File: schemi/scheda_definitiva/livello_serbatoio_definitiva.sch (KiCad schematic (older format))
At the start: 43 parts, among them J1 USB_B, J2 BTN_LED_GROUP, J3 CONN_LCD, J4 CONN_US, J5 ICSP, J6 Exp_Analog_2, J7 Exp_Analog, SW1 SW_RST, U1 FT232RL, U2 ATmega328P-PU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

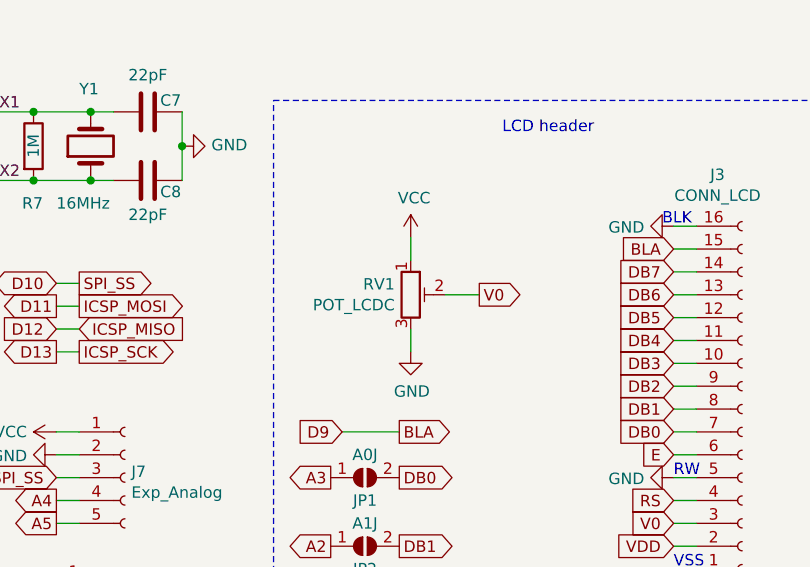
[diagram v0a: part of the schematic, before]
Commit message: spostato LCD e rifatto modello box - LCD centrato su LCD - revisione layout - nuovo modello box (box + coperchio + pulsante + assembly scheda e lcd) - aggiornate immagini prototipo - creati file stl (box e coperchio)  per preventivazione stampa 3d
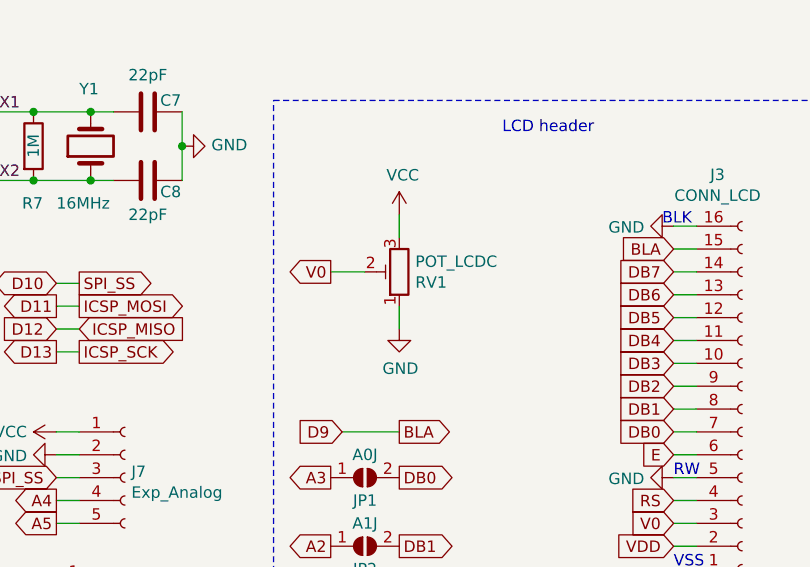
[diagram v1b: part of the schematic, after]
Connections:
- net GND: now also RV1.1; no longer RV1.3
- net VCC: now also RV1.3; no longer RV1.1
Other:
- moved on the sheet: RV1
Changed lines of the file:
@@
 L power:VCC #PWR015
 U 1 1 5F56E79B
-P 9100 3200
-F 0 "#PWR015" H 9100 3050 50  0001 C CNN
-F 1 "VCC" H 9115 3373 50  0000 C CNN
-F 2 "" H 9100 3200 50  0001 C CNN
-F 3 "" H 9100 3200 50  0001 C CNN
-	1    9100 3200
+P 9050 3100
+F 0 "#PWR015" H 9050 2950 50  0001 C CNN
+F 1 "VCC" H 9065 3273 50  0000 C CNN
+F 2 "" H 9050 3100 50  0001 C CNN
+F 3 "" H 9050 3100 50  0001 C CNN
+	1    9050 3100
 	1    0    0    -1
 $EndComp
@@
 D5
 Wire Wire Line
-	9100 3600 9100 3700
+	9050 3200 9050 3100
 Wire Wire Line
-	9250 3450 9400 3450
+	8900 3350 8750 3350
 Wire Wire Line
-	9100 3200 9100 3300
-Text GLabel 9400 3450 2    50   Output ~ 0
+	9050 3600 9050 3500
+Text GLabel 8750 3350 0    50   Output ~ 0
 V0
 Wire Wire Line
@@
 L Device:R_POT_TRIM RV1
 U 1 1 5F0B6050
-P 9100 3450
-F 0 "RV1" H 9030 3496 50  0000 R CNN
-F 1 "POT_LCDC" H 9030 3405 50  0000 R CNN
-F 2 "simboli_custom:Trimmer_ACP_470" H 9100 3450 50  0001 C CNN
-F 3 "~" H 9100 3450 50  0001 C CNN
-	1    9100 3450
-	1    0    0    -1
+P 9050 3350
+F 0 "RV1" H 8980 3396 50  0000 R CNN
+F 1 "POT_LCDC" H 8980 3305 50  0000 R CNN
+F 2 "simboli_custom:Trimmer_ACP_470" H 9050 3350 50  0001 C CNN
+F 3 "~" H 9050 3350 50  0001 C CNN
+	1    9050 3350
+	-1   0    0    1
 $EndComp
 $Comp
 L power:GND #PWR016
 U 1 1 5F0B54BC
-P 9100 3700
-F 0 "#PWR016" H 9100 3450 50  0001 C CNN
-F 1 "GND" H 9105 3527 50  0000 C CNN
-F 2 "" H 9100 3700 50  0001 C CNN
-F 3 "" H 9100 3700 50  0001 C CNN
-	1    9100 3700
+P 9050 3600
+F 0 "#PWR016" H 9050 3350 50  0001 C CNN
+F 1 "GND" H 9055 3427 50  0000 C CNN
+F 2 "" H 9050 3600 50  0001 C CNN
+F 3 "" H 9050 3600 50  0001 C CNN
+	1    9050 3600
 	1    0    0    -1
 $EndComp

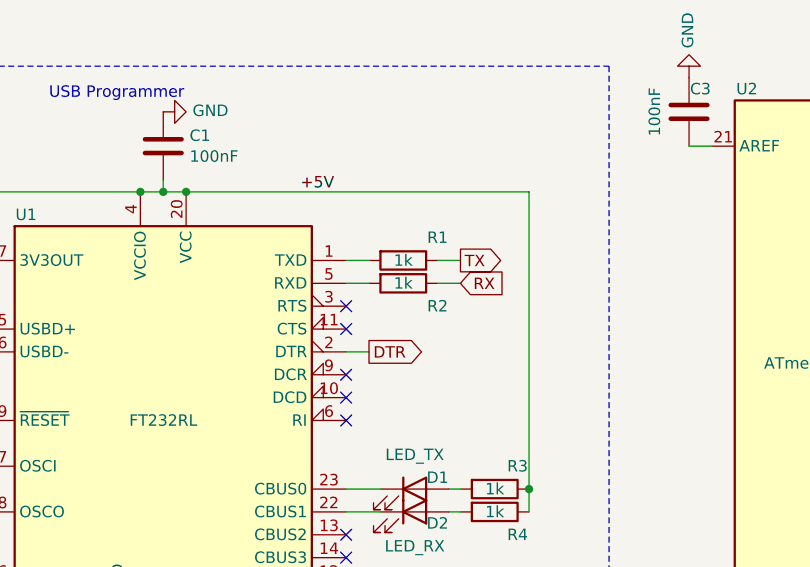
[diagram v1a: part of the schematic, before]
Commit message: aggiunte piazzole CTS/RTS + aggiunte etichette a pin digitali - rivisto gerber - rivista footprint oscillatore
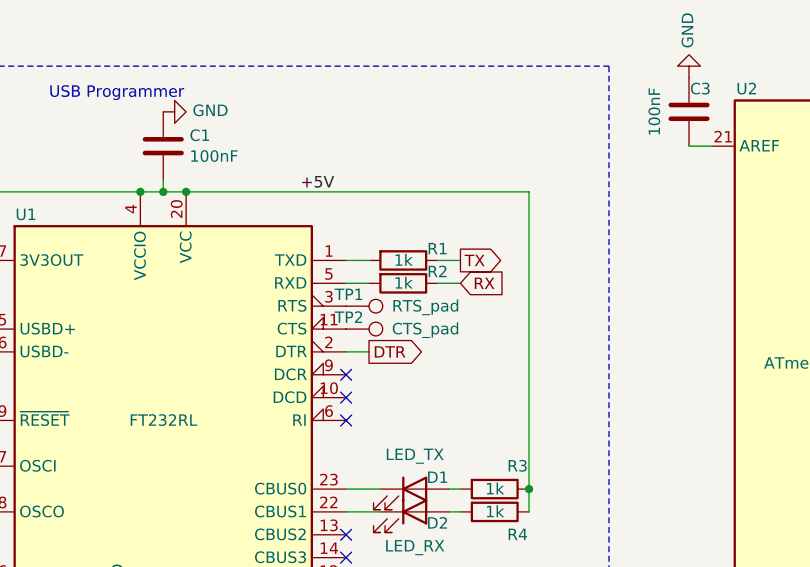
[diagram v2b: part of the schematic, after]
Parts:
- added TP1: RTS_pad, TestPoint:TestPoint_Pad_D1.0mm, symbol Connector:TestPoint
- added TP2: CTS_pad, TestPoint:TestPoint_Pad_D1.0mm, symbol Connector:TestPoint
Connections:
- net at U1.11 (CTS): now also TP2.1
- net at U1.3 (RTS): now also TP1.1
- no-connect marks 10 -> 8
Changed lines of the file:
@@
 Sheet 1 1
 Title "Monitor Serbatoio"
-Date "2020-11-21"
-Rev "1"
+Date "2020-12-27"
+Rev "v1.0_Rev.A"
 Comp ""
-Comment1 ""
+Comment1 "Versione Espandibile"
 Comment2 ""
 Comment3 ""
@@
 U 1 1 5F436A47
 P 4100 2750
-F 0 "R2" V 4200 2900 50  0000 C CNN
+F 0 "R2" V 4050 2900 50  0000 C CNN
 F 1 "1k" V 4100 2750 50  0000 C CNN
 F 2 "Resistor_THT:R_Axial_DIN0309_L9.0mm_D3.2mm_P12.70mm_Horizontal" V 4030 2750 50  0001 C CNN
@@
 U 1 1 5F435E22
 P 4100 2650
-F 0 "R1" V 4000 2800 50  0000 C CNN
+F 0 "R1" V 4050 2800 50  0000 C CNN
 F 1 "1k" V 4100 2650 50  0000 C CNN
 F 2 "Resistor_THT:R_Axial_DIN0309_L9.0mm_D3.2mm_P12.70mm_Horizontal" V 4030 2650 50  0001 C CNN
@@
 	1    0    0    -1
 $EndComp
-NoConn ~ 3850 2850
-NoConn ~ 3850 2950
 NoConn ~ 3850 3150
 NoConn ~ 3850 3250
@@
 Text Notes 7800 700  0    50   ~ 0
 Button + LED
+$Comp
+L Connector:TestPoint TP1
+U 1 1 5FE956AB
+P 3850 2850
+F 0 "TP1" V 3800 2800 50  0000 L CNN
+F 1 "RTS_pad" V 3850 3050 50  0000 L CNN
+F 2 "TestPoint:TestPoint_Pad_D1.0mm" H 4050 2850 50  0001 C CNN
+F 3 "~" H 4050 2850 50  0001 C CNN
+	1    3850 2850
+	0    1    1    0
+$EndComp
+$Comp
+L Connector:TestPoint TP2
+U 1 1 5FE99EB0
+P 3850 2950
+F 0 "TP2" V 3800 2900 50  0000 L CNN
+F 1 "CTS_pad" V 3850 3150 50  0000 L CNN
+F 2 "TestPoint:TestPoint_Pad_D1.0mm" H 4050 2950 50  0001 C CNN
+F 3 "~" H 4050 2950 50  0001 C CNN
+	1    3850 2950
+	0    1    1    0
+$EndComp
 $EndSCHEMATC

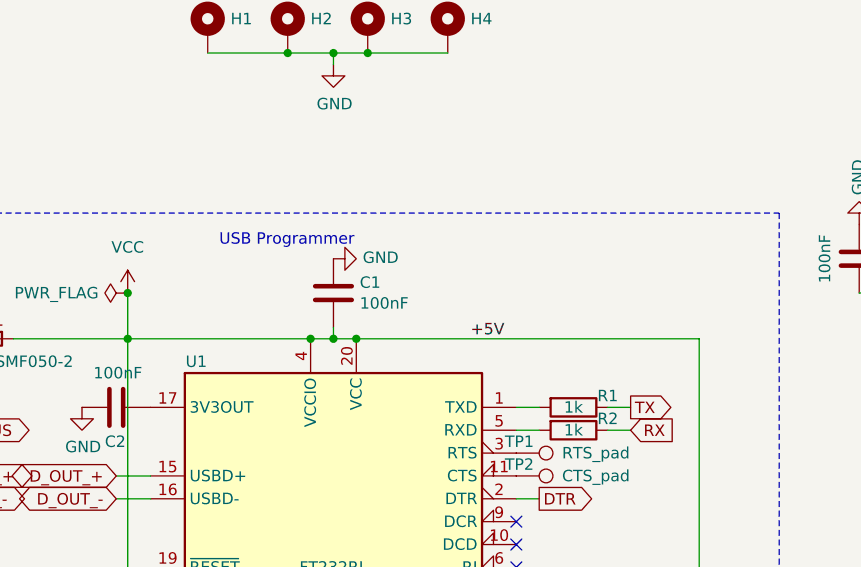
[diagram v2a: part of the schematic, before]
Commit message: modifica per seriale - aggiunto elettrolitico per alimentazione - fix test seriale
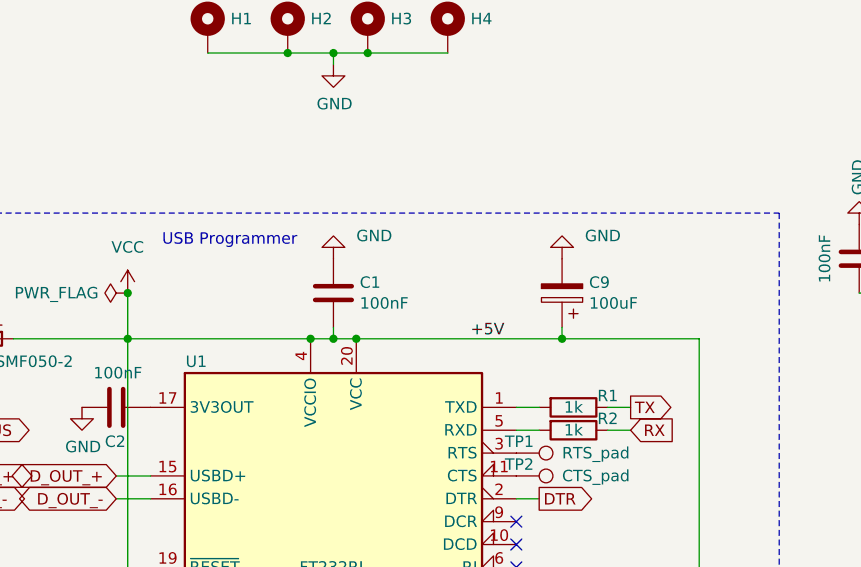
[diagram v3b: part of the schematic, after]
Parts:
- added C9: 100uF, Capacitor_THT:CP_Radial_D5.0mm_P2.00mm, symbol Device:CP
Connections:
- net GND: now also C9.2
- net VCC: now also C9.1
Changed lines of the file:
@@
 Sheet 1 1
 Title "Monitor Serbatoio"
-Date "2020-12-27"
-Rev "v1.0_Rev.A"
+Date "2021-02-13"
+Rev "v1.0_Rev.B"
 Comp ""
 Comment1 "Versione Espandibile"
@@
 Text GLabel 4350 2650 2    50   Output ~ 0
 TX
-Text Notes 2550 1950 0    50   ~ 0
+Text Notes 2300 1950 0    50   ~ 0
 USB Programmer
 Connection ~ 2150 2150
@@
 Wire Wire Line
 	4650 2350 4650 3650
-Wire Wire Line
-	3150 2350 4650 2350
 Wire Wire Line
 	4000 3750 3850 3750
@@
 P 3050 2000
 F 0 "#PWR0104" H 3050 1750 50  0001 C CNN
-F 1 "GND" V 3055 1872 50  0000 R CNN
+F 1 "GND" H 2950 1900 50  0000 R CNN
 F 2 "" H 3050 2000 50  0001 C CNN
 F 3 "" H 3050 2000 50  0001 C CNN
 	1    3050 2000
-	0    -1   -1   0
+	-1   0    0    1
 $EndComp
 $Comp
@@
 	0    1    1    0
 $EndComp
+$Comp
+L Device:CP C9
+U 1 1 60287C39
+P 4050 2150
+F 0 "C9" H 3932 2104 50  0000 R CNN
+F 1 "100uF" H 3932 2195 50  0000 R CNN
+F 2 "Capacitor_THT:CP_Radial_D5.0mm_P2.00mm" H 4088 2000 50  0001 C CNN
+F 3 "~" H 4050 2150 50  0001 C CNN
+	1    4050 2150
+	-1   0    0    1
+$EndComp
+$Comp
+L power:GND #PWR026
+U 1 1 6029B133
+P 4050 2000
+F 0 "#PWR026" H 4050 1750 50  0001 C CNN
+F 1 "GND" H 3950 1900 50  0000 R CNN
+F 2 "" H 4050 2000 50  0001 C CNN
+F 3 "" H 4050 2000 50  0001 C CNN
+	1    4050 2000
+	-1   0    0    1
+$EndComp
+Wire Wire Line
+	3150 2350 4050 2350
+Wire Wire Line
+	4050 2300 4050 2350
+Connection ~ 4050 2350
+Wire Wire Line
+	4050 2350 4650 2350
 $EndSCHEMATC

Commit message: aggiunta ferrite a scheda rev. B
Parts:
- added FB1: MPZ2012, Inductor_SMD:L_0805_2012Metric_Pad1.15x1.40mm_HandSolder, symbol Device:Ferrite_Bead
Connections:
- net VBUS: now also FB1.1; no longer J1.1 (VBUS)
- new net: FB1.2, J1.1 (VBUS)
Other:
- moved on the sheet: F1
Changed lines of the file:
@@
 	0    -1   -1   0
 $EndComp
-Wire Wire Line
-	1250 2750 1300 2750
-Connection ~ 1300 2750
-Wire Wire Line
-	1300 2350 1300 2750
 $Comp
 L Device:R R9
@@
 DTR
 Wire Wire Line
-	1650 2350 2150 2350
-Wire Wire Line
 	2150 2150 2150 2350
 NoConn ~ 2250 3750
@@
 Wire Wire Line
 	2250 3350 2150 3350
-Wire Wire Line
-	1300 2350 1350 2350
 $Comp
 L Device:C C2
@@
 Text GLabel 1350 3050 2    50   BiDi ~ 0
 D_IN_-
-Text GLabel 1400 2750 2    50   BiDi ~ 0
-VBUS
 Text GLabel 2100 2950 0    50   BiDi ~ 0
 D_OUT_+
@@
 Text GLabel 2050 5700 2    50   BiDi ~ 0
 D_OUT_-
-Wire Wire Line
-	1300 2750 1400 2750
 Wire Wire Line
 	1250 2950 1350 2950
@@
 L Device:Polyfuse F1
 U 1 1 5FB200DA
-P 1500 2350
-F 0 "F1" V 1400 2350 50  0000 C CNN
-F 1 "MF-MSMF050-2" V 1600 2500 50  0000 C CNN
-F 2 "simboli_custom:MF-MSMF_1812_4532Metric_Pad1.30x3.40mm_HandSolder" H 1550 2150 50  0001 L CNN
-F 3 "~" H 1500 2350 50  0001 C CNN
-	1    1500 2350
+P 1700 2350
+F 0 "F1" V 1600 2350 50  0000 C CNN
+F 1 "MF-MSMF050-2" V 1800 2350 50  0000 C CNN
+F 2 "simboli_custom:MF-MSMF_1812_4532Metric_Pad1.30x3.40mm_HandSolder" H 1750 2150 50  0001 L CNN
+F 3 "~" H 1700 2350 50  0001 C CNN
+	1    1700 2350
 	0    1    1    0
 $EndComp
@@
 Wire Wire Line
 	4050 2350 4650 2350
+$Comp
+L Device:Ferrite_Bead FB1
+U 1 1 6044950F
+P 1400 2750
+F 0 "FB1" V 1250 2750 50  0000 C CNN
+F 1 "MPZ2012" V 1500 2950 50  0000 C CNN
+F 2 "Inductor_SMD:L_0805_2012Metric_Pad1.15x1.40mm_HandSolder" V 1330 2750 50  0001 C CNN
+F 3 "~" H 1400 2750 50  0001 C CNN
+	1    1400 2750
+	0    1    1    0
+$EndComp
+Text GLabel 1600 2750 2    50   BiDi ~ 0
+VBUS
+Wire Wire Line
+	1600 2750 1550 2750
+Connection ~ 1550 2750
+Wire Wire Line
+	1550 2350 1550 2750
+Wire Wire Line
+	1850 2350 2150 2350
 $EndSCHEMATC

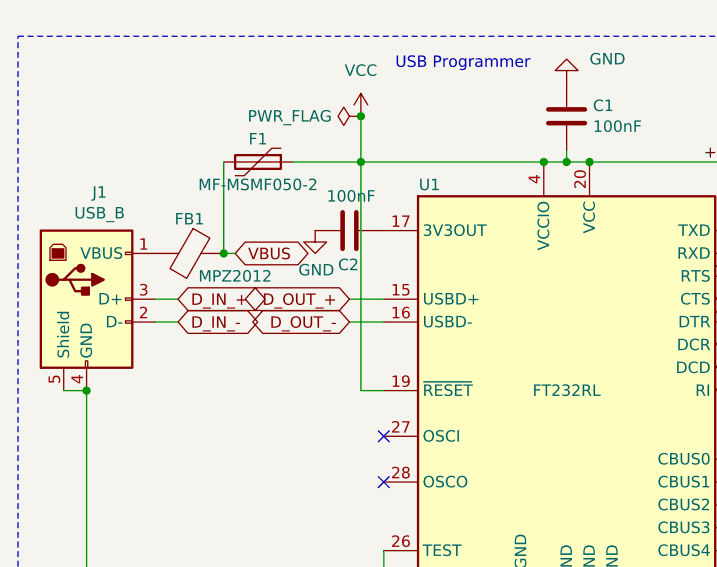
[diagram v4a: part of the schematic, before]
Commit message: disconnesso pin reset di ft232
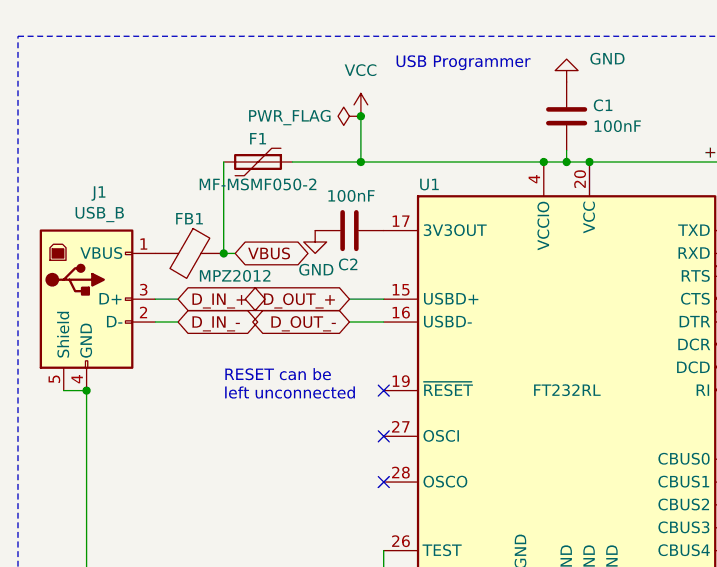
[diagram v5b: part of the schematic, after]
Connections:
- net VCC: no longer U1.19 (~RESET~)
- no-connect marks 8 -> 9
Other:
- note added: "RESET can be \nleft unconnected"
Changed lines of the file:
@@
 NoConn ~ 2250 3550
 Connection ~ 2150 2350
-Wire Wire Line
-	2150 3350 2150 2350
-Wire Wire Line
-	2250 3350 2150 3350
 $Comp
 L Device:C C2
@@
 Wire Wire Line
 	1850 2350 2150 2350
+NoConn ~ 2250 3350
+Text Notes 1550 3400 0    50   ~ 0
+RESET can be \nleft unconnected
 $EndSCHEMATC
